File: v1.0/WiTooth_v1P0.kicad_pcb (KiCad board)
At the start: 2 copper layers, 48 parts, among them P2 JTAG, P3 CONN_01X04, P4 CONN_01X20, P5 CONN_01X20, Q1 Q_NPN_EBC, Q2 Q_NPN_EBC, SW1 RESET, SW2 Switch_SPDT_x2, SW3 USER_SW, U1 AMS1117-3V3, U2 CP2102

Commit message: initial placement started
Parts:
- removed C14: 100uF, Capacitors_SMD:C_1206_HandSoldering
- removed C15: 1uF, Capacitors_SMD:C_0805_HandSoldering
- removed R17: 0E, Resistors_SMD:R_0805_HandSoldering
- added P1: USB_A_MALE, USB:usb-PCB_male, F.Cu at (-26.2, 48.5)
- added U3: ESP-32_WROOM32_Rectangle, ESP-32:ESP32-WROOM, F.Cu at (312.9, 145.8)
- added Y1: Crystal, Crystals:Crystal_AT310_d3.0mm_l10.0mm_Horizontal_1EP_style1, F.Cu at (304.3, 20.1)
- C1: value 0.1uF -> 10uF
- C12: value 1nF -> 100uF; footprint Capacitors_SMD:C_0805_HandSoldering -> Capacitors_SMD:C_1206_HandSoldering
- C13: value 27pF -> 1uF
- C3: value DNM -> 47pF
- C4: value 47pF -> 10uF
- C5: value 47uF -> 47pF
- C6: value 47pF -> 1uF
- C7: value 22uF -> 1nF
- C8: value 1uF -> 1nF
- C9: value 1nF -> 27pF
- R10: value 12K -> 5K
- R11: value 5K -> 470E
- R12: value 1K -> 470E
- R13: value 470E -> 5K
- R14: value 10K -> 470E
- R15: value 470E -> 0E
- R4: value 27E -> 1K
- R5: value 1K -> 27E
- R6: value 5K -> 12K
- R7: value 12K -> 470E
- U1: footprint TO_SOT_Packages_SMD:SOT-223-3Lead_TabPin2 -> TO_SOT_Packages_SMD:SOT-223
- moved P2 284.3 mm to (314.5, 111.8)
- moved P3 244.2 mm to (331.2, 120.7)
- moved P5 231.1 mm to (339.1, 125.2)
- moved P4 215.0 mm to (293.4, 126.7)
- moved C11 196.9 mm to (297.4, 18.8), turned to 90 degrees
- moved R16 196.1 mm to (297.4, 23.6)
- moved D5 118.0 mm to (331.7, 54.4)
- moved R11 103.7 mm to (332.0, 52.1)
- moved R10 102.2 mm to (332.0, 49.0)
- moved C12 87.4 mm to (331.5, 41.1), turned to 180 degrees
- moved C10 87.4 mm to (332.0, 46.5)
- moved R14 81.2 mm to (332.2, 43.9)
- moved R13 81.1 mm to (301.5, 75.4)
- moved R15 79.9 mm to (308.9, 23.6), turned to 90 degrees
- moved R7 77.5 mm to (301.8, 79.8), turned to 180 degrees
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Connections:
- C10 pad 1: EN -> IO34
- C12 pad 1: IO34 -> +3V3
- C13 pad 1: Net-(C13-Pad1) -> +3V3
- C3 pad 1: +5V -> Net-(C3-Pad1)
- C4 pad 1: Net-(C4-Pad1) -> +3V3
- C5 pad 1: +3V3 -> Net-(C5-Pad1)
- C6 pad 1: Net-(C6-Pad1) -> +5V
- C7 pad 1: +3V3 -> EN
- C8 pad 1: +5V -> EN
- C9 pad 1: EN -> Net-(C9-Pad1)
- P2 pad 7: Net-(P2-Pad7) -> (no net)
- R10 pad 1: Net-(D4-Pad1) -> IO2
- R10 pad 2: IO32 -> GND
- R11 pad 1: IO2 -> Net-(D5-Pad1)
- R12 pad 1: Net-(D5-Pad1) -> +3V3
- R12 pad 2: GND -> EN
- R13 pad 1: +3V3 -> Net-(R13-Pad1)
- R13 pad 2: EN -> +3V3
- R14 pad 2: Net-(R14-Pad2) -> IO34
- R15 pad 1: +3V3 -> IO32
- R15 pad 2: IO34 -> Net-(C9-Pad1)
- R16 pad 1: IO32 -> IO33
- R3 pad 2: Net-(C4-Pad1) -> Net-(C3-Pad1)
- R4 pad 1: Net-(R4-Pad1) -> Net-(D1-Pad1)
- R4 pad 2: Net-(C6-Pad1) -> GND
- R5 pad 1: Net-(D1-Pad1) -> Net-(R5-Pad1)
- R5 pad 2: GND -> Net-(C5-Pad1)
- R6 pad 2: IO0 -> EN
- R7 pad 1: +3V3 -> Net-(D4-Pad1)
- R7 pad 2: EN -> IO27
- SW2 pad 1: Net-(R14-Pad2) -> Net-(R13-Pad1)
- U2 pad 1: Net-(U2-Pad1) -> (no net)
- U2 pad 10: Net-(U2-Pad10) -> (no net)
- U2 pad 11: Net-(U2-Pad11) -> (no net)
- U2 pad 12: Net-(U2-Pad12) -> (no net)
- U2 pad 13: Net-(U2-Pad13) -> (no net)
- U2 pad 14: Net-(U2-Pad14) -> (no net)
- U2 pad 15: Net-(U2-Pad15) -> (no net)
- U2 pad 16: Net-(U2-Pad16) -> (no net)
- U2 pad 17: Net-(U2-Pad17) -> (no net)
- U2 pad 18: Net-(U2-Pad18) -> (no net)
- U2 pad 19: Net-(U2-Pad19) -> (no net)
- U2 pad 2: Net-(U2-Pad2) -> (no net)
- U2 pad 20: Net-(U2-Pad20) -> (no net)
- U2 pad 21: Net-(U2-Pad21) -> (no net)
- U2 pad 22: Net-(U2-Pad22) -> (no net)
- U2 pad 23: CTS -> (no net)
- U2 pad 27: Net-(U2-Pad27) -> (no net)
- U2 pad 29: GND -> Net-(U2-Pad29)
- U2 pad 3: GND -> Net-(U2-Pad29)
- U2 pad 5: Net-(R4-Pad1) -> Net-(R5-Pad1)
- U2 pad 9: Net-(U2-Pad9) -> (no net)

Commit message: basic placement done
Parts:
- C12, C13, P2, R10: moved to B.Cu
- U3: footprint ESP-32:ESP32-WROOM -> ESP-32:ESP32-WROOM_SMALLER_FOOTPRINT
- moved R14 204.1 mm to (135.1, 96.7), turned to 90 degrees
- moved R11 200.1 mm to (135.9, 91.8), turned to 180 degrees
- moved C10 197.8 mm to (140.7, 96.7), turned to 270 degrees
- moved D5 195.1 mm to (140.2, 91.8)
- moved SW3 195.1 mm to (137.9, 96.4)
- moved R10 191.0 mm to (149.6, 105.7)
- moved R6 179.6 mm to (122.4, 84.7)
- moved D4 179.6 mm to (122.4, 82.8)
- moved C12 179.5 mm to (161.0, 97.4), turned to 270 degrees
- moved P2 176.7 mm to (138.1, 100.4)
- moved C9 176.5 mm to (142.7, 78.1)
- moved P5 176.1 mm to (163.5, 111.4), turned to 270 degrees
- moved R7 174.8 mm to (127.0, 82.8), turned to 0 degrees
- moved Y1 174.1 mm to (140.7, 79.6)
- moved R15 173.2 mm to (144.4, 78.0), turned to 270 degrees
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
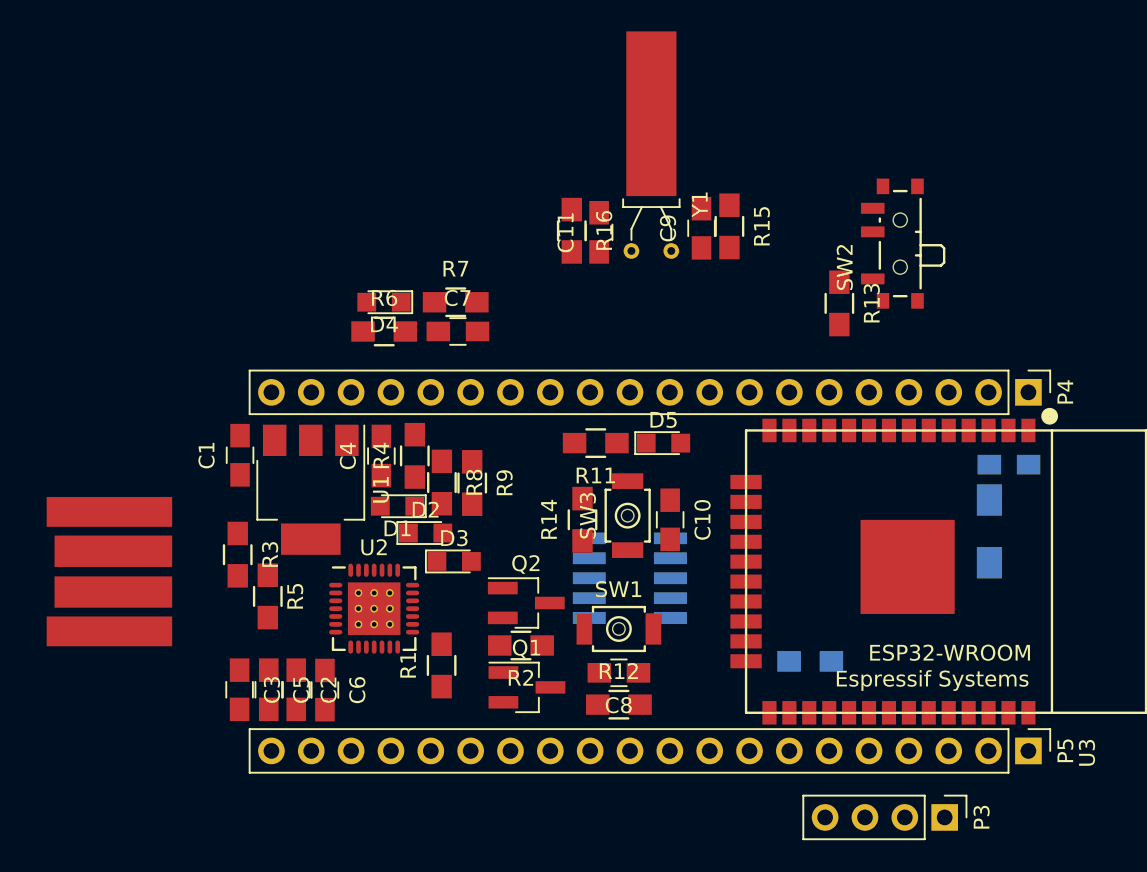
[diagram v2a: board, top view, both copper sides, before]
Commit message: schematic updated and some parts removed; layout work started
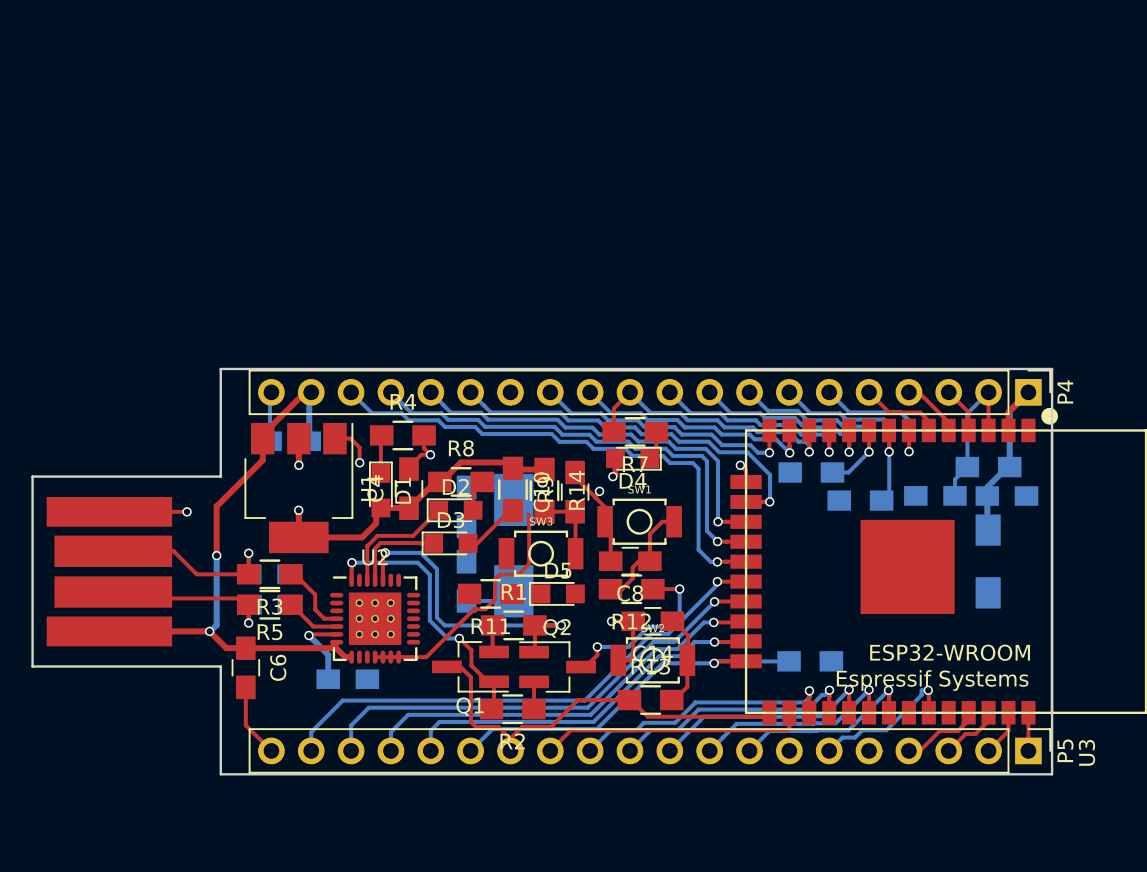
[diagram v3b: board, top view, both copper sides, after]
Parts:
- removed P2: JTAG, Pin_Headers:Pin_Header_Straight_2x05_Pitch1.27mm_SMD
- removed P3: CONN_01X04, Pin_Headers:Pin_Header_Straight_1x04_Pitch2.54mm
- added C14: 1nF, Capacitors_SMD:C_0805_HandSoldering, F.Cu at (139.5, 103.2)
- C1, C11, C2, C3, C5, C7, C9, R15, R16, R6: moved to B.Cu
- R13: value 5K -> 470E
- SW1, SW3: footprint switches:SW_SPST_B3U-1000P-B_SUNROM -> switches:SW_SPST_B3U-1000P_SUNROM
- SW2: value Switch_SPDT_x2 -> BOOT; footprint Buttons_Switches_SMD:SW_SPDT_PCM12 -> switches:SW_SPST_B3U-1000P_SUNROM
- Y1: footprint Crystals:Crystal_AT310_d3.0mm_l10.0mm_Horizontal_1EP_style1 -> Crystals:Crystal_SMD_0603-2pin_6.0x3.5mm_HandSoldering; moved to B.Cu
- moved R6 39.5 mm to (160.9, 93.3), turned to 180 degrees
- moved C7 32.2 mm to (157.6, 95.2), turned to 180 degrees
- moved SW2 30.7 mm to (139.5, 105.7), turned to 0 degrees
- moved R13 28.0 mm to (139.4, 108.2), turned to 0 degrees
- moved C9 27.0 mm to (127.7, 100.6)
- moved R16 21.7 mm to (149.7, 93.7), turned to 180 degrees
- moved Y1 21.3 mm to (130.7, 98.3), turned to 90 degrees
- moved C11 19.4 mm to (127.7, 95.9), turned to 270 degrees
- moved R15 19.4 mm to (152.8, 95.5), turned to 180 degrees
- moved D4 18.7 mm to (138.3, 92.8)
- moved R7 14.1 mm to (138.4, 91.1), turned to 180 degrees
- moved D5 11.7 mm to (133.5, 101.4)
- moved R11 11.7 mm to (129.2, 101.4)
- moved C3 7.60 mm to (115.1, 100.2), turned to 0 degrees
- moved R12 7.41 mm to (138.2, 101.1), turned to 180 degrees
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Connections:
- C8 pad 1: EN -> Net-(C8-Pad1)
- R12 pad 1: +3V3 -> EN
- R12 pad 2: EN -> Net-(C8-Pad1)
- R13 pad 1: Net-(R13-Pad1) -> IO0
- R13 pad 2: +3V3 -> Net-(C14-Pad1)
- SW1 pad 2: EN -> Net-(C8-Pad1)
- SW2 pad 1: Net-(R13-Pad1) -> GND
- SW2 pad 2: IO0 -> Net-(C14-Pad1)
- U2 pad 29: Net-(U2-Pad29) -> GND
- U2 pad 3: Net-(U2-Pad29) -> GND
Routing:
- net +5V: track 0.00 -> 37.9 mm, vias 0 -> 2
- net +3V3: track 0.00 -> 36.2 mm, vias 0 -> 3
- net GND: track 0.00 -> 34.3 mm, vias 0 -> 6
- net CLK: track 0.00 -> 33.0 mm, vias 0 -> 1
- net CMD: track 0.00 -> 32.7 mm, vias 0 -> 1
- net SD0: track 0.00 -> 30.1 mm, vias 0 -> 1
- net SD3: track 0.00 -> 29.2 mm, vias 0 -> 1
- net IO0: track 0.00 -> 27.4 mm
- net SD1: track 0.00 -> 26.8 mm, vias 0 -> 1
- net SD2: track 0.00 -> 25.8 mm, vias 0 -> 1
- net IO2: track 0.00 -> 24.8 mm, vias 0 -> 1
- net IO13: track 0.00 -> 24.5 mm, vias 0 -> 1
- net IO15: track 0.00 -> 23.7 mm, vias 0 -> 1
- net EN: track 0.00 -> 21.2 mm, vias 0 -> 2
- net RTS: track 0.00 -> 20.2 mm, vias 0 -> 2
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- added copper zone on 3V3, net +3V3
- added copper zone on GND, net GND
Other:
- board outline added: 65 x 25.8 mm
- copper layers 2 -> 4
- net class Default: trace_width 0.25 -> 0.254
- net class POWER added: clearance 0.2, trace_width 0.381, via_dia 0.6, via_drill 0.4

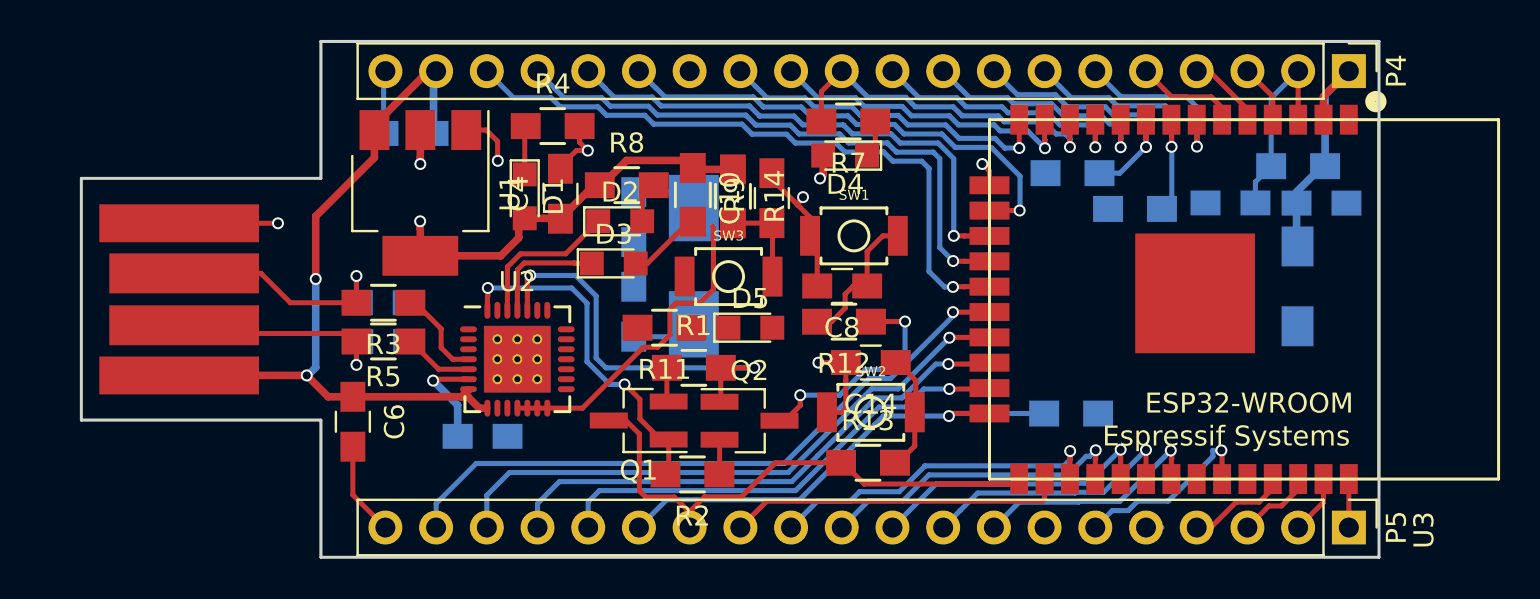
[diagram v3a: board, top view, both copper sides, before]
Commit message: Routing completed for all
Routing completed for all
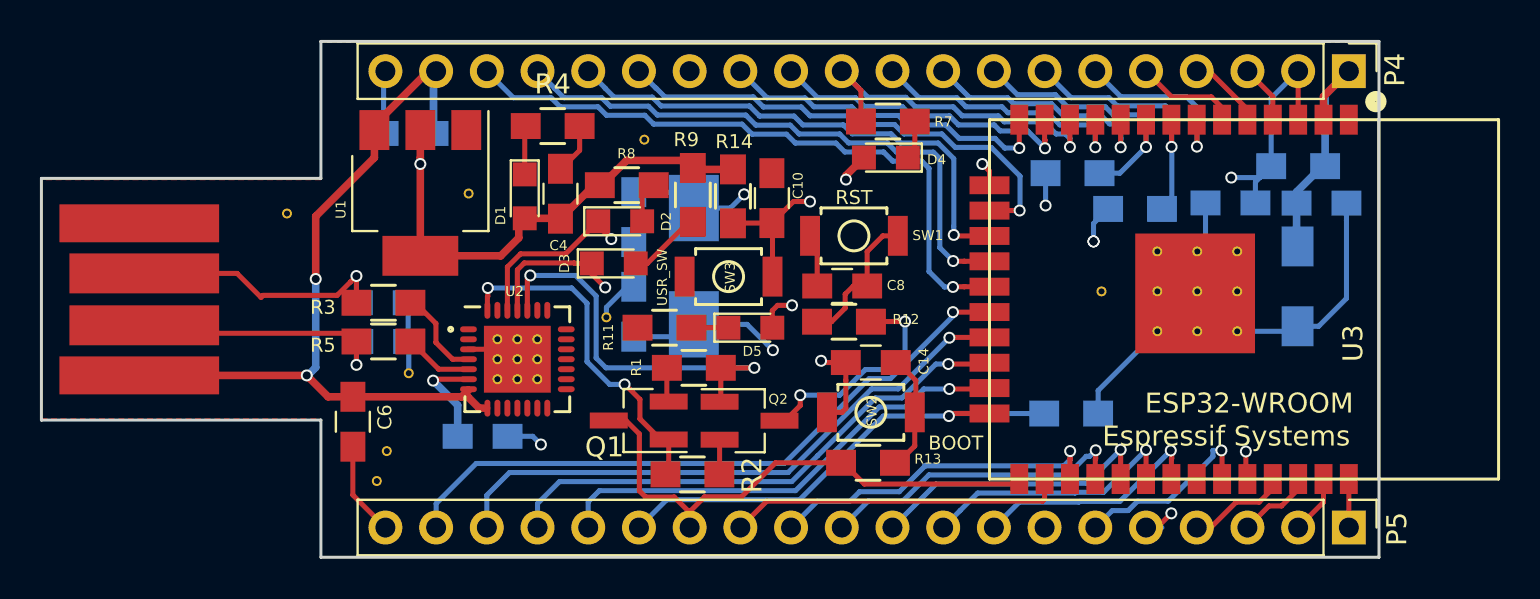
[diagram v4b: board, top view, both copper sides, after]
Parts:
- added G***: LOGO, logos:thingTronics_10mm, B.Cu at (147.4, 100.0)
- added REF**: VIA_0.5mm, via:VIA_0.5mm, F.Cu at (151.1, 99.6)
- added REF**: VIA_0.5mm, via:VIA_0.5mm, F.Cu at (157.9, 99.6)
- added REF**: VIA_0.5mm, via:VIA_0.5mm, F.Cu at (155.9, 99.6)
- added REF**: VIA_0.5mm, via:VIA_0.5mm, F.Cu at (153.9, 99.6)
- added REF**: VIA_0.5mm, via:VIA_0.5mm, F.Cu at (157.9, 97.6)
- added REF**: VIA_0.5mm, via:VIA_0.5mm, F.Cu at (155.9, 97.6)
- added REF**: VIA_0.5mm, via:VIA_0.5mm, F.Cu at (153.9, 97.6)
- added REF**: VIA_0.5mm, via:VIA_0.5mm, F.Cu at (128.2, 92.0)
- added REF**: VIA_0.5mm, via:VIA_0.5mm, F.Cu at (110.3, 95.7)
- added REF**: VIA_0.5mm, via:VIA_0.5mm, F.Cu at (115.3, 107.6)
- added REF**: VIA_0.5mm, via:VIA_0.5mm, F.Cu at (114.8, 109.1)
- added REF**: VIA_0.5mm, via:VIA_0.5mm, F.Cu at (126.3, 100.9)
- added REF**: VIA_0.5mm, via:VIA_0.5mm, F.Cu at (116.4, 103.7)
- added REF**: VIA_0.5mm, via:VIA_0.5mm, F.Cu at (119.4, 94.7)
- added REF**: VIA_0.5mm, via:VIA_0.5mm, F.Cu at (157.9, 101.6)
- added REF**: VIA_0.5mm, via:VIA_0.5mm, F.Cu at (155.9, 101.6)
- added REF**: VIA_0.5mm, via:VIA_0.5mm, F.Cu at (153.9, 101.6)
- moved D4 2.04 mm to (140.3, 92.9)
- moved P1 2.00 mm to (98.0, 100.0)
- moved R7 1.98 mm to (140.4, 91.1)
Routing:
- net RXD0: track 8.78 -> 56.1 mm, vias 0 -> 3
- net TXD0: track 11.0 -> 49.4 mm, vias 0 -> 1
- net Net-(C9-Pad1): track 3.27 -> 28.3 mm, vias 0 -> 3
- net GND: track 34.3 -> 58.4 mm, vias 6 -> 3
- net IO35: track 9.17 -> 31.6 mm, vias 1 -> 2
- net IO34: track 10.3 -> 32.2 mm, vias 0 -> 1
- net EN: track 21.2 -> 42.8 mm, vias 2 -> 3
- net Net-(C11-Pad1): track 3.81 -> 24.4 mm, vias 0 -> 2
- net (no net): track 16.2 -> 0.00 mm
- net +3V3: track 36.2 -> 39.3 mm, vias 3 -> 2
- net Net-(C5-Pad1): track 11.3 -> 13.9 mm
- net Net-(C3-Pad1): track 11.9 -> 14.3 mm
- net +5V: track 37.9 -> 39.9 mm
- net Net-(D5-Pad1): track 0.00 -> 1.85 mm
- added copper zone on F.Cu, net GND
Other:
- board size 65 x 25.8 mm -> 67 x 25.8 mm
- board text added: "BOOT"
- board text added: "RST"
- board text added: "USR_SW"
- board text added: "WiTooth v1.0"
